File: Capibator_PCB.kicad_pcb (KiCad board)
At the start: 2 copper layers, 116 parts, among them J1 FTDI, J10 mist, J12 Water_Level, J13 Main_Input_Jack, J14 Battery, J15 Display, J16 Conn_01x05, J17 Temp, J18 Temp2, J19 Water_Pump, J2 LED, J20 Conn_01x04_Socket, J21 extra, J3 C8465, J4 C8465, J5 Screw_Terminal_01x02, J6 C8465, J7 Screw_Terminal_01x02, J8 Fan_Exhaust, J9 Fan_Continous, K1 G5NB-1A-E DC12, Q10 AO3406, Q2 AO3406, Q3 AO3406, Q4 AO3406, Q5 AO3406, Q6 AO3406, Q7 SI2301, Q8 AO3406, Q9 AO3406, SW1 SW_Omron_B3FS, SW2 SW_Omron_B3FS, U1 TPS63070RNMR, U2 ESP32-WROOM-32, U3 AMS1117-5.0, U5 PCF8574, U6 MAX17048G_T10, U7 TP4056, U8 DS1307+, U9 G5NB-1A-E DC12, Y1 32.768kHz Quartz Crystal

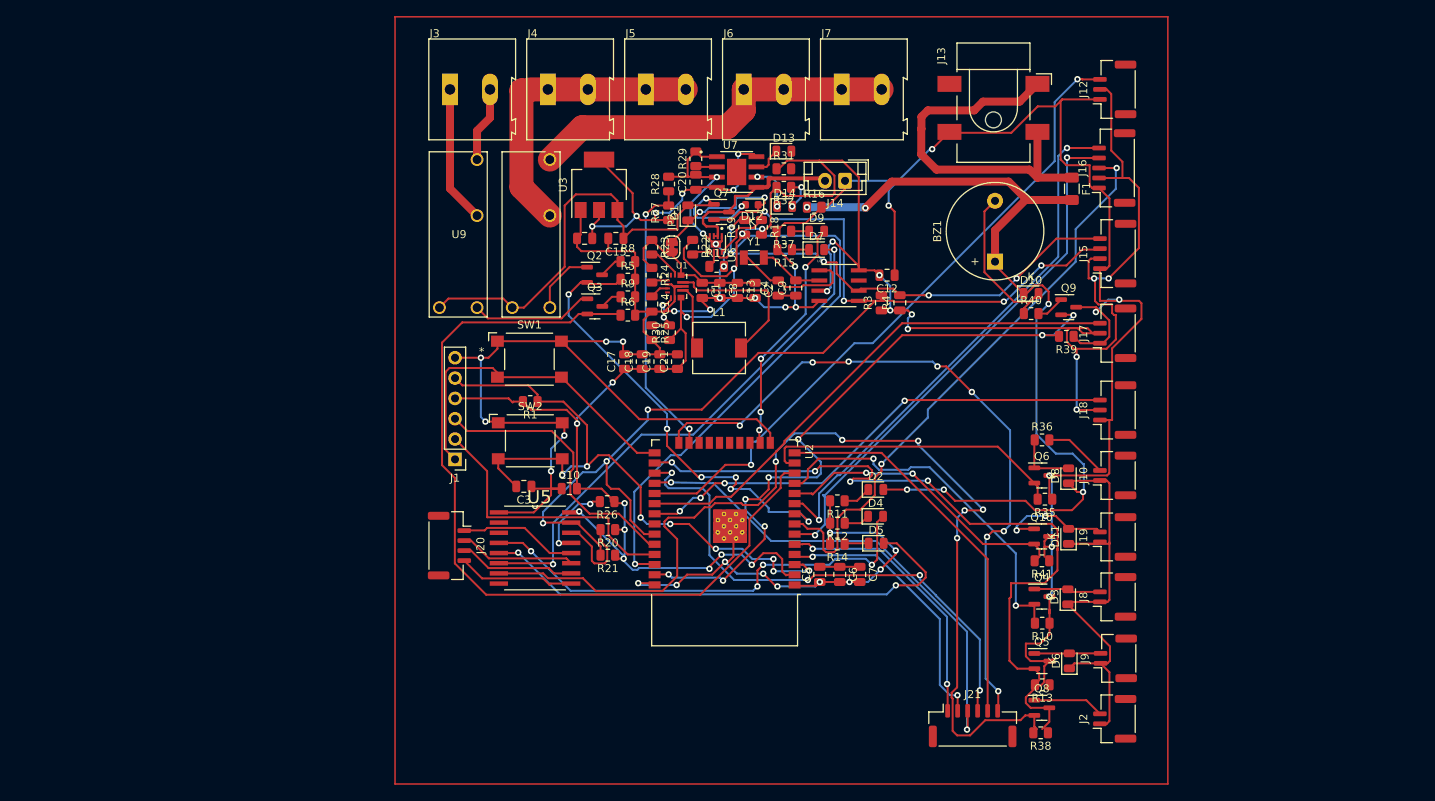
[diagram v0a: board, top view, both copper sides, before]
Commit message: started version 2, better placements without routing
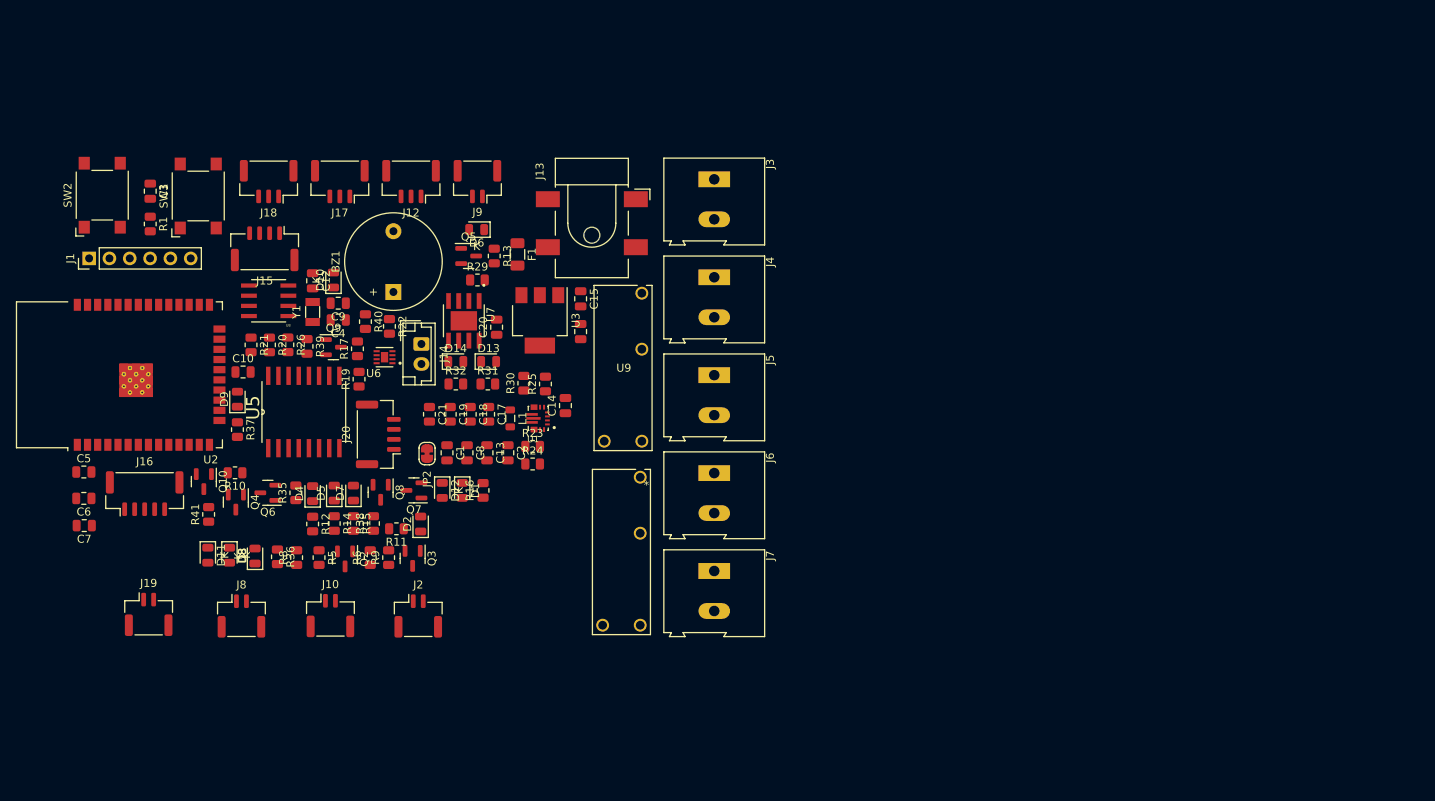
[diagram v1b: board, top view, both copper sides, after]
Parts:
- removed J21: extra, Connector_JST:JST_GH_SM06B-GHS-TB_1x06-1MP_P1.25mm_Horizontal
- removed R18, R27: 10k, Resistor_SMD:R_0805_2012Metric
- removed R28: 20k, Resistor_SMD:R_0805_2012Metric
- removed R3, R4: 10k, Capacitor_SMD:C_0805_2012Metric
- D12: footprint Diode_SMD:D_0603_1608Metric -> Diode_SMD:D_0805_2012Metric
- J15, J20: footprint Connector_JST:JST_GH_SM04B-GHS-TB_1x04-1MP_P1.25mm_Horizontal -> Connector_JST:JST_GH_BM04B-GHS-TBT_1x04-1MP_P1.25mm_Vertical
- J16: value Conn_01x05 -> Rotary encoder; footprint Connector_JST:JST_GH_SM05B-GHS-TB_1x05-1MP_P1.25mm_Horizontal -> Connector_JST:JST_GH_BM05B-GHS-TBT_1x05-1MP_P1.25mm_Vertical
- L1: footprint Inductor_SMD:L_6.3x6.3_H3 -> Inductor_SMD:L_0805_2012Metric
- moved J16 127.8 mm to (69.3, 101.6), turned to 0 degrees
- moved J19 121.1 mm to (69.8, 116.7), turned to 0 degrees
- moved J18 109.5 mm to (84.8, 62.6), turned to 180 degrees
- moved J8 109.2 mm to (81.4, 116.9), turned to 0 degrees
- moved D11 107.6 mm to (77.2, 109.3), turned to -90 degrees
- moved J15 106.3 mm to (84.3, 71.0), turned to 180 degrees
- moved Q10 104.9 mm to (76.7, 100.1), turned to -90 degrees
- moved D3 104.9 mm to (79.9, 109.3), turned to -90 degrees
- moved R41 104.3 mm to (77.3, 104.2), turned to 90 degrees
- moved R10 102.6 mm to (80.6, 99.0)
- moved D8 102.2 mm to (83.1, 109.4)
- moved Q4 101.4 mm to (80.7, 102.7), turned to -90 degrees
- moved J10 99.6 mm to (92.5, 116.8), turned to 0 degrees
- moved J9 99.5 mm to (110.9, 62.6), turned to 180 degrees
- moved J17 98.7 mm to (93.7, 62.6), turned to 180 degrees
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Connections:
- J16 pad 3: /MCU/ROT_SW -> /MCU/ROTARY_CLK
- J16 pad 4: /MCU/ROTARY_CLK -> /MCU/ROT_SW
- J20 pad 1: /MCU/P_IO_6 -> /MCU/FAN_CON_PIN
- J20 pad 4: /MCU/P_IO_4 -> /MCU/BUZ_PIN
- U2 pad 12: /MCU/turner -> /MCU/MIST_PIN
- U2 pad 13: /MCU/MIST_PIN -> /MCU/turner
- U2 pad 26: /MCU/FAN_CON_PIN -> unconnected-(U2-IO4-Pad26)
- U2 pad 37: /MCU/BUZ_PIN -> unconnected-(U2-IO23-Pad37)
- U5 pad 12: /MCU/P_IO_6 -> /MCU/FAN_CON_PIN
- U5 pad 9: /MCU/P_IO_4 -> /MCU/BUZ_PIN
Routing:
- net GND: track 469.8 -> 0.00 mm, vias 34 -> 0
- net +3.3V: track 311.2 -> 0.00 mm, vias 23 -> 0
- net +12V: track 242.7 -> 0.00 mm, vias 8 -> 0
- net /MCU/SDA: track 142.4 -> 0.00 mm, vias 7 -> 0
- net /MCU/SCL: track 141.9 -> 0.00 mm, vias 6 -> 0
- net /MCU/LED_PIN: track 126.8 -> 0.00 mm, vias 6 -> 0
- net /MCU/turner: track 105.3 -> 0.00 mm
- net /MCU/GPIO2: track 88.8 -> 0.00 mm, vias 8 -> 0
- net /MCU/FAN_CON_PIN: track 87.2 -> 0.00 mm, vias 4 -> 0
- net /MCU/BUZ_PIN: track 84.2 -> 0.00 mm, vias 8 -> 0
- net /MCU/WATER_LEVEL_DATA: track 83.2 -> 0.00 mm, vias 2 -> 0
- net /MCU/RESET: track 82.2 -> 0.00 mm, vias 8 -> 0
- net /MCU/ROT_SW: track 73.5 -> 0.00 mm, vias 2 -> 0
- net /MCU/ROTARY_DATA: track 67.6 -> 0.00 mm, vias 2 -> 0
- net /MCU/ROTARY_CLK: track 67.2 -> 0.00 mm, vias 2 -> 0
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
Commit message: changed picture in readme
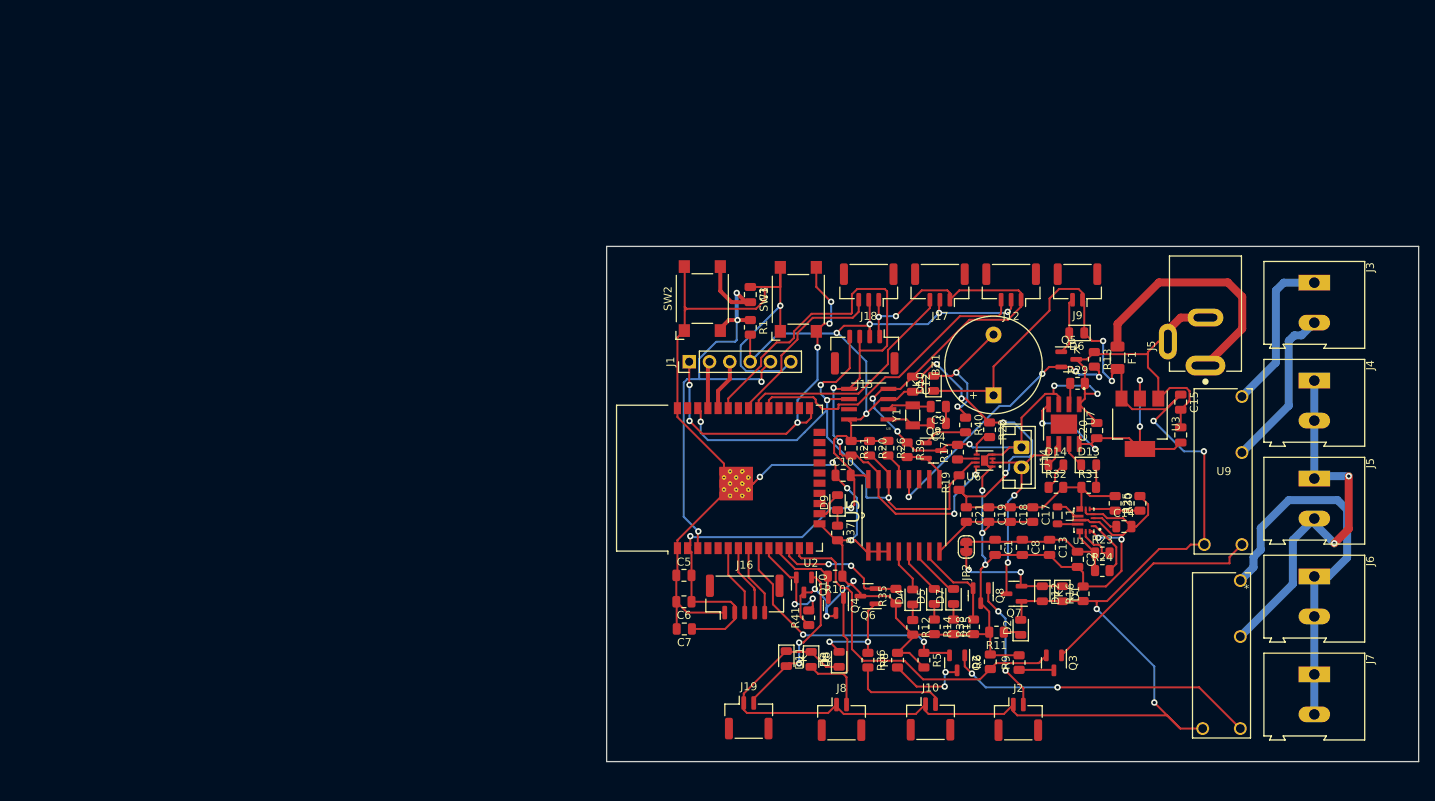
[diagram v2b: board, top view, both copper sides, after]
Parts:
- removed J13: Main_Input_Jack, Connector_BarrelJack:BarrelJack_CLIFF_FC681465S_SMT_Horizontal
- removed J20: Conn_01x04_Socket, Connector_JST:JST_GH_BM04B-GHS-TBT_1x04-1MP_P1.25mm_Vertical
- added J5: PJ-002AH, PJ-002AH:CUI_PJ-002AH, F.Cu at (201.9, 85.6)
- moved Q3 81.2 mm to (183.0, 122.8)
- moved R9 79.9 mm to (178.6, 122.7)
- moved R6 78.6 mm to (175.0, 122.6)
- moved Q2 77.6 mm to (170.9, 122.8)
- moved R5 76.7 mm to (166.7, 122.4)
- moved R31 76.2 mm to (187.3, 100.8)
- moved R8 76.2 mm to (163.4, 122.4)
- moved C10 76.1 mm to (156.6, 99.3)
- moved J12 76.1 mm to (177.6, 75.5)
- moved R10 76.1 mm to (155.6, 111.9)
- moved R16 76.1 mm to (186.6, 114.1)
- moved R19 76.1 mm to (171.1, 100.2)
- moved R21 76.1 mm to (157.6, 95.9)
- moved R39 76.1 mm to (164.6, 96.1)
- moved C12 76.1 mm to (165.3, 87.9)
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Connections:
- U2 pad 8: /MCU/heater -> /MCU/ROTARY_DATA
- U2 pad 9: /MCU/ROTARY_DATA -> /MCU/heater
- U9 pad 2: Net-(J3-Pin_1) -> Net-(J3-Pin_2)
- U9 pad 3: Net-(J3-Pin_2) -> Net-(J3-Pin_1)
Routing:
- net GND: track 0.00 -> 423.0 mm, vias 0 -> 20
- net +12V: track 0.00 -> 207.2 mm, vias 0 -> 6
- net +3.3V: track 0.00 -> 195.9 mm, vias 0 -> 11
- net /MCU/SDA: track 0.00 -> 83.6 mm, vias 0 -> 4
- net /MCU/SCL: track 0.00 -> 75.1 mm, vias 0 -> 4
- net /MCU/RESET: track 0.00 -> 62.9 mm, vias 0 -> 4
- net Net-(J6-Pin_1): track 0.00 -> 48.7 mm
- net Net-(J4-Pin_1): track 0.00 -> 48.5 mm, vias 0 -> 2
- net /MCU/GPIO0: track 0.00 -> 47.8 mm, vias 0 -> 6
- net /MCU/turner: track 0.00 -> 45.0 mm
- net Net-(Q2-D): track 0.00 -> 39.0 mm, vias 0 -> 2
- net /MCU/WATER_LEVEL_DATA: track 0.00 -> 37.9 mm
- net +5V: track 0.00 -> 36.3 mm, vias 0 -> 4
- net /MCU/FAN_CON_PIN: track 0.00 -> 34.8 mm, vias 0 -> 4
- net /MCU/heater: track 0.00 -> 33.3 mm, vias 0 -> 2
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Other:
- board outline added: 101.5 x 64.4 mm

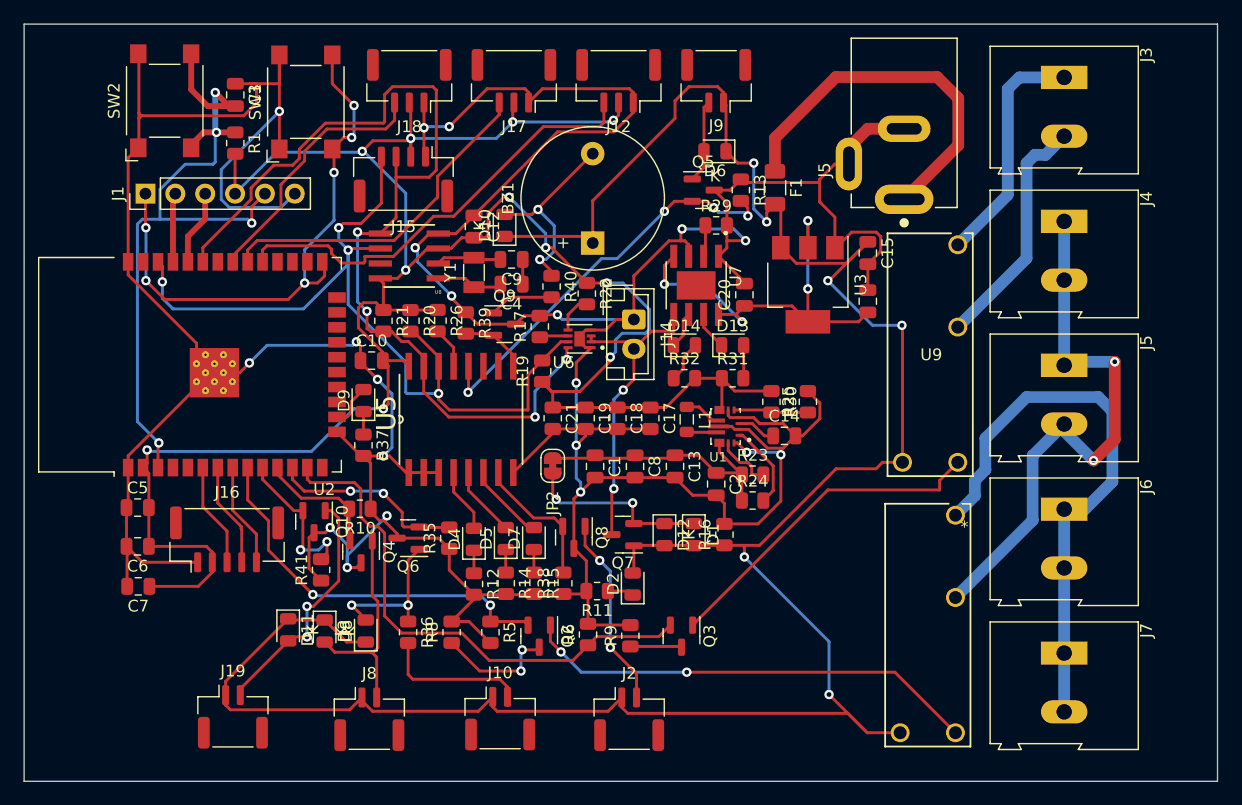
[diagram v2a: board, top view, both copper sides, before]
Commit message: generated bom for jlcpcb
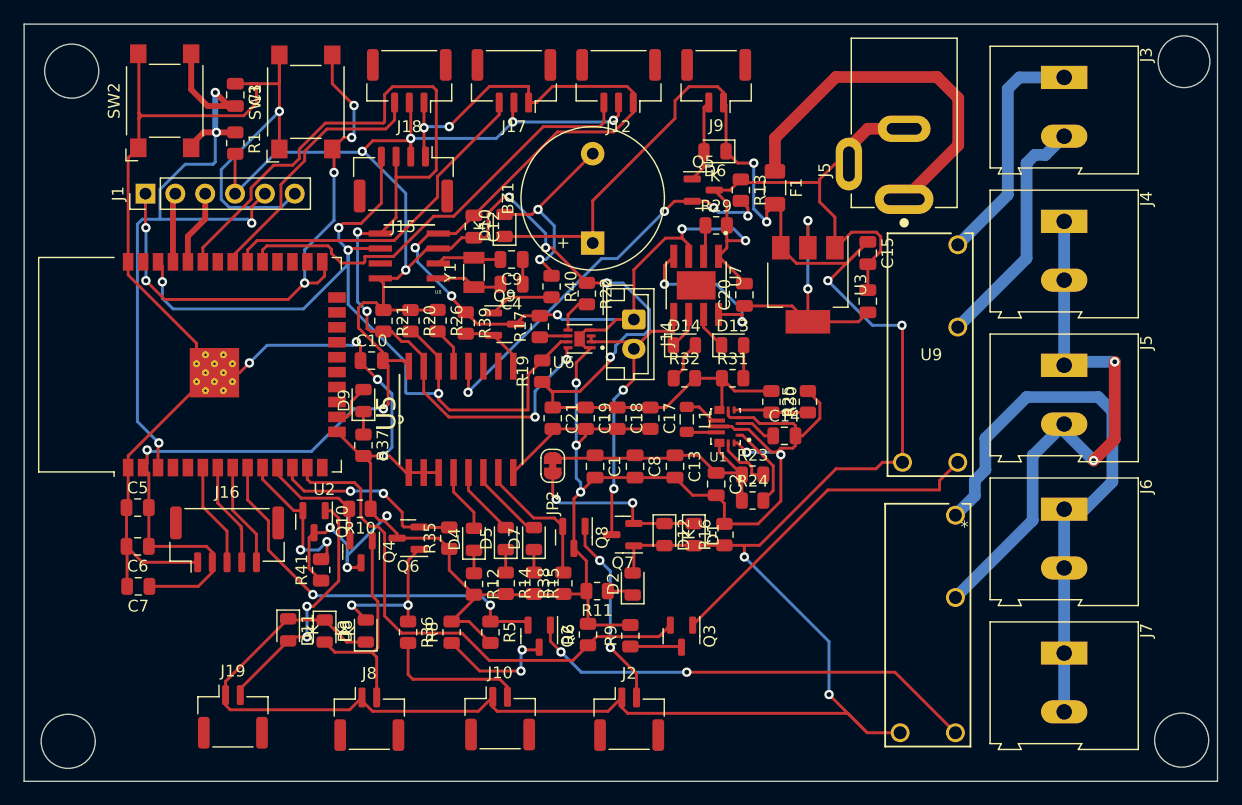
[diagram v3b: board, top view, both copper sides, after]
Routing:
- net GND: track 423.0 -> 425.2 mm
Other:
- outline, holes or cut-outs redrawn
